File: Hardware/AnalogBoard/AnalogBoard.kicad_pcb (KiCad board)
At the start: 2 copper layers, 11 parts, among them P1 CONN_4, P2 ACH67, P3 ACH45, P4 ACH23, P5 ACH01, U1 10uf, U2 0.1uf, U3 0.1uf, U4 10uf, U5 LTC2309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

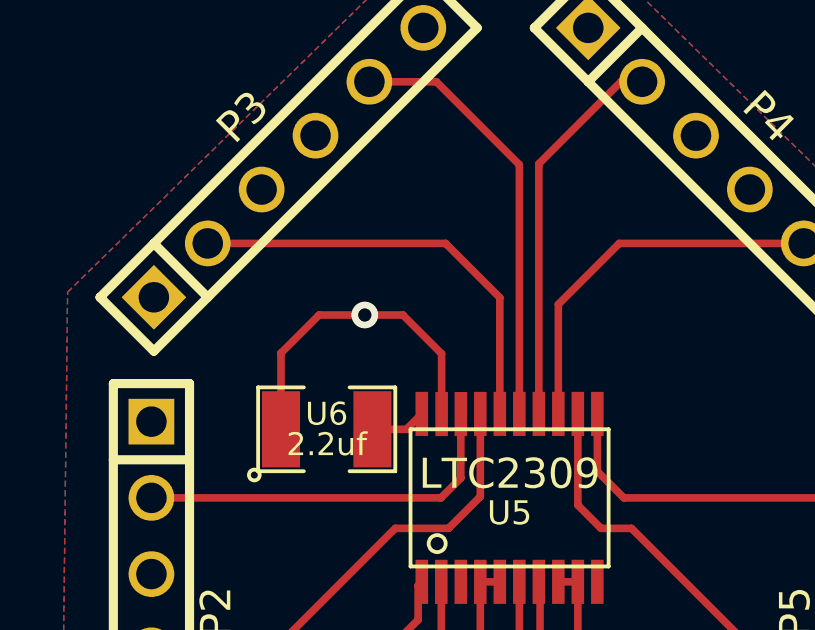
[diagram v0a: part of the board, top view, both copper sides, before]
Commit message: Changing VIA Size for the Analog Board Moving Analog Board away from Digital board connector
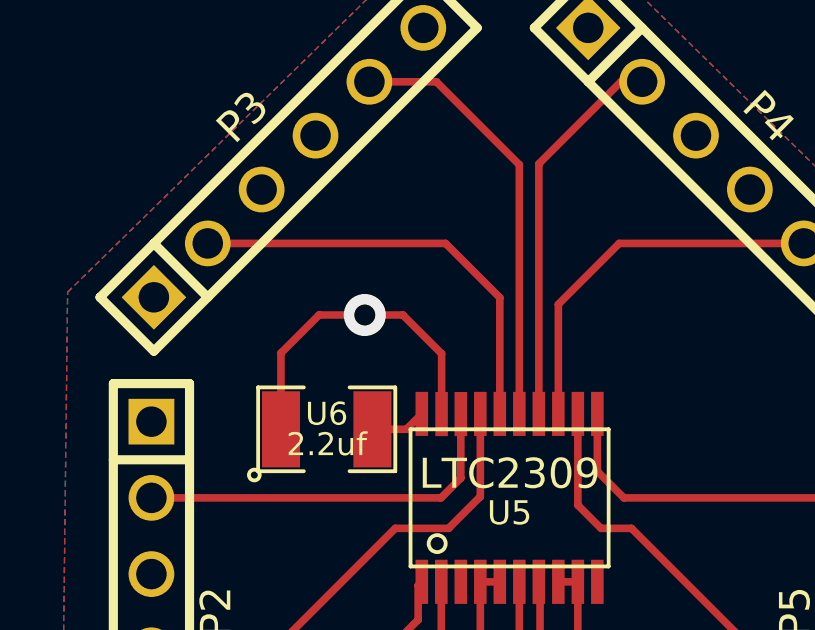
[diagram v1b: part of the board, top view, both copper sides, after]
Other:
- net class Default: via_dia 0.889 -> 1.4; via_drill 0.635 -> 1
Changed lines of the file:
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@@
     (links 44)
     (no_connects 1)
-    (area 28.448 51.816 61.468001 92.710001)
+    (area 30.226 52.832 59.9186 92.3036)
     (thickness 1.6)
     (drawings 0)
@@
     (segment_width 0.2)
     (edge_width 0.1)
-    (via_size 0.889)
-    (via_drill 0.635)
+    (via_size 1.4)
+    (via_drill 1)
     (via_min_size 0.889)
     (via_min_drill 0.508)
-    (uvia_size 0.508)
-    (uvia_drill 0.127)
+    (uvia_size 1.4)
+    (uvia_drill 1)
     (uvias_allowed no)
     (uvia_min_size 0.508)
@@
     (pad_to_mask_clearance 0)
     (aux_axis_origin 0 0)
-    (visible_elements FFFFFFBF)
+    (visible_elements 7FFFFFFF)
     (pcbplotparams
       (layerselection 3178497)
@@
     (clearance 0.254)
     (trace_width 0.254)
-    (via_dia 0.889)
-    (via_drill 0.635)
-    (uvia_dia 0.508)
-    (uvia_drill 0.127)
+    (via_dia 1.4)
+    (via_drill 1)
+    (uvia_dia 1.4)
+    (uvia_drill 1)
     (add_net "")
     (add_net +5V)
@@
   (segment (start 42.94632 66.56832) (end 41.656 65.278) (width 0.254) (layer F.Cu) (net 2))
   (segment (start 41.656 65.278) (end 40.386 65.278) (width 0.254) (layer F.Cu) (net 2))
-  (via (at 40.386 65.278) (size 0.889) (layers F.Cu B.Cu) (net 2))
+  (via (at 40.386 65.278) (size 1.4) (layers F.Cu B.Cu) (net 2))
   (segment (start 42.94632 66.56832) (end 42.94632 68.58) (width 0.254) (layer F.Cu) (net 2))
   (segment (start 38.862 65.278) (end 40.386 65.278) (width 0.254) (layer F.Cu) (net 2))

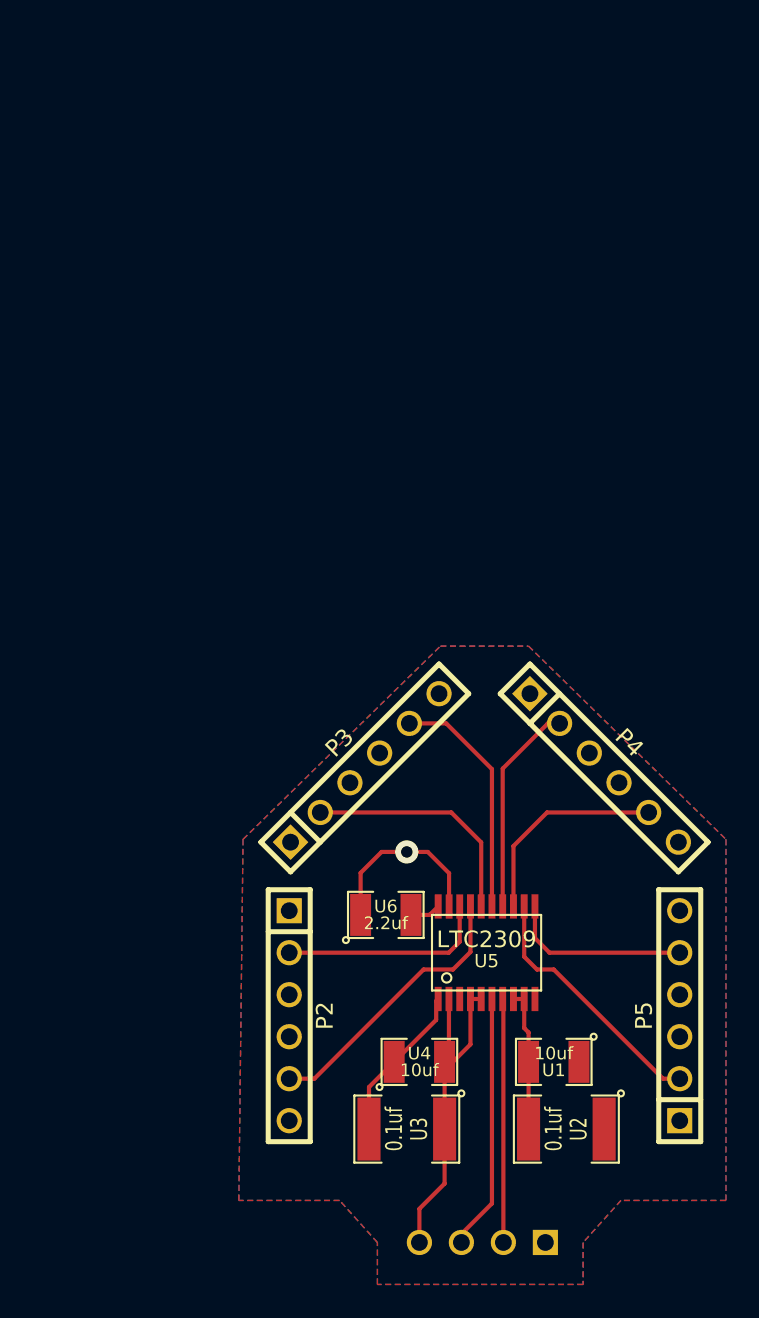
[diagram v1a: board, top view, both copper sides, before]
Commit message: Updated PCB to make it more DIY friendly Changed Vsense pin to A3 Added Design Folder
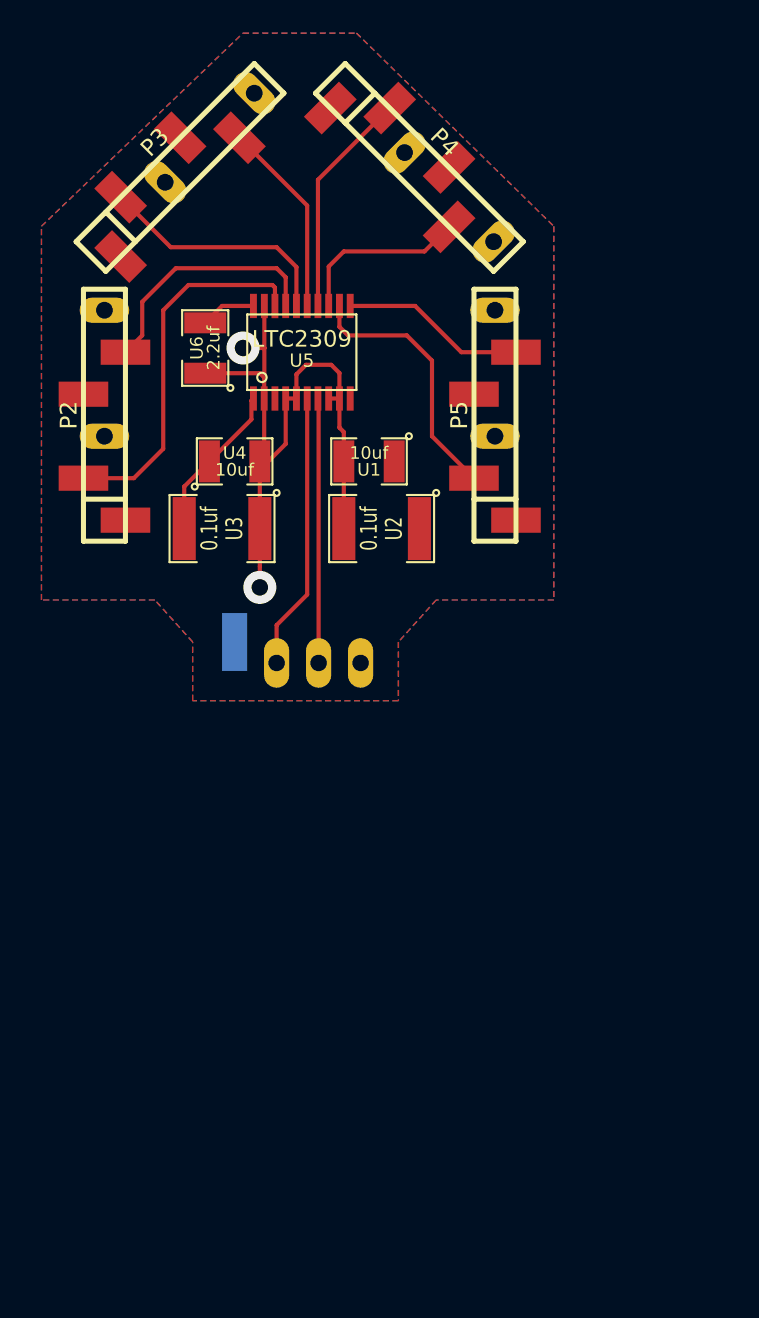
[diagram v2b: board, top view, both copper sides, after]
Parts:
- P1: footprint PIN_ARRAY_4x1 -> PIN_ARRAY_4x1_MIXED_INV
- P2, P3, P4, P5: footprint PIN_ARRAY-6X1 -> PIN_ARRAY-6X1_MIXED
- moved U3 38.0 mm to (29.2, 45.7)
- moved P2 38.0 mm to (22.1, 38.9), turned to 90 degrees
- moved P5 38.0 mm to (45.7, 38.9)
- moved U1 38.0 mm to (38.1, 41.7)
- moved U4 38.0 mm to (30.0, 41.7)
- moved U5 38.0 mm to (34.0, 35.1)
- moved P3 38.0 mm to (26.7, 23.9)
- moved P4 38.0 mm to (41.1, 23.9)
- moved U2 38.0 mm to (38.9, 45.7)
- moved P1 36.8 mm to (33.8, 53.8)
- moved U6 36.0 mm to (28.2, 34.8), turned to 90 degrees
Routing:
- net N-0000012: track 12.7 -> 22.5 mm
- net N-000005: track 14.4 -> 11.9 mm
- net N-000006: track 12.7 -> 10.7 mm
- net N-000003: track 16.9 -> 14.9 mm
- net GND: track 40.5 -> 42.2 mm, vias 1 -> 2
- net N-000008: track 1.86 -> 3.34 mm
- net SCL: track 15.5 -> 16.8 mm
- net SDA: track 14.7 -> 16.0 mm
- net N-000002: track 12.9 -> 13.8 mm
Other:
- net class Default: via_dia 1.4 -> 2

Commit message: * Updating PCB to more rectangular + Caps + On/Off Switch * Disabling Digital Breakout board for now
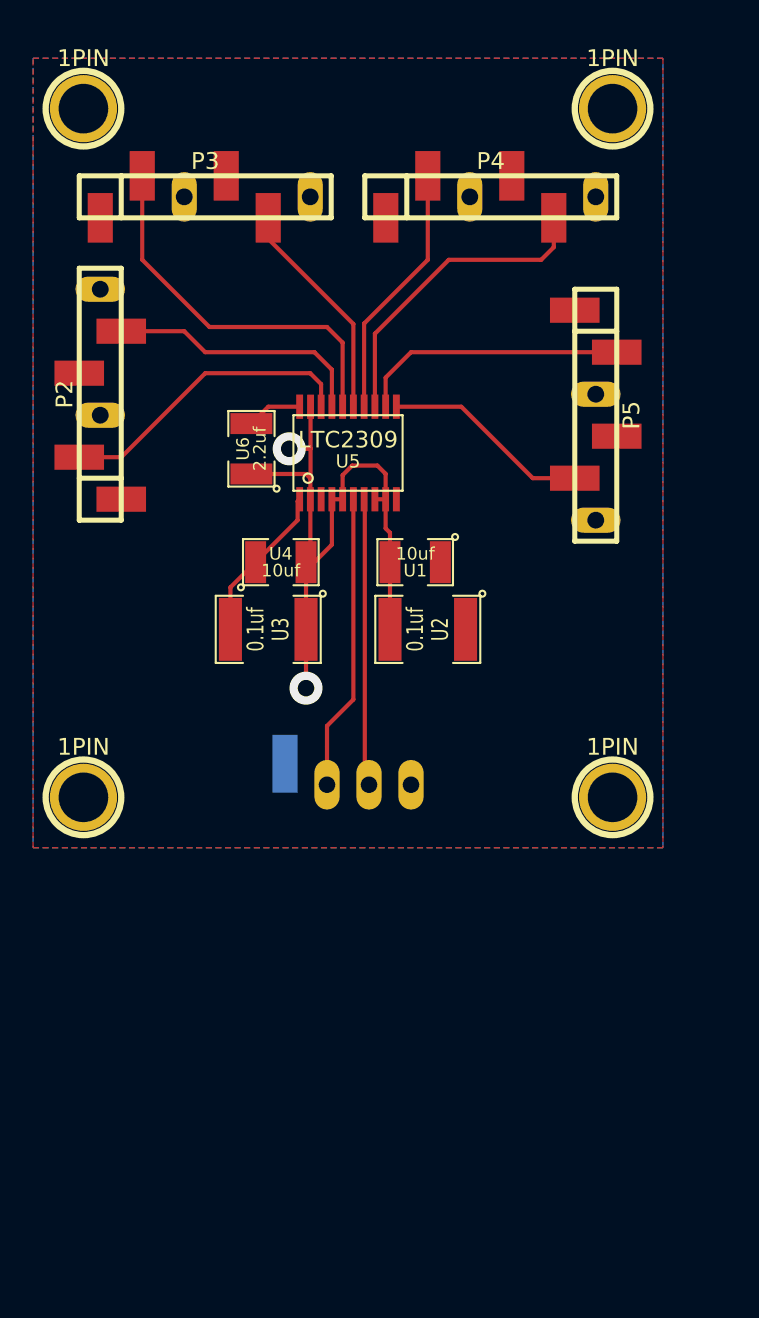
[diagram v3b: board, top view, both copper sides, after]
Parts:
- added 1PIN: P***, 1pin, F.Cu at (52.8, 62.0)
- added 1PIN: P***, 1pin, F.Cu at (20.8, 62.0)
- added 1PIN: P***, 1pin, F.Cu at (52.8, 20.3)
- added 1PIN: P***, 1pin, F.Cu at (20.8, 20.3)
- moved P1 7.97 mm to (36.8, 61.2)
- moved U1 6.71 mm to (40.9, 47.8)
- moved U2 6.71 mm to (41.7, 51.8)
- moved U3 6.71 mm to (32.0, 51.8)
- moved U4 6.71 mm to (32.8, 47.8)
- moved U5 6.71 mm to (36.8, 41.1)
- moved U6 6.71 mm to (31.0, 40.9)
- moved P5 6.10 mm to (51.8, 38.9), turned to 270 degrees
- moved P4 4.67 mm to (45.5, 25.7), turned to 0 degrees
- moved P3 2.34 mm to (28.2, 25.7), turned to 0 degrees
- moved P2 1.30 mm to (21.8, 37.6)
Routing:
- net N-000006: track 10.7 -> 19.2 mm
- net N-000004: track 14.7 -> 23.2 mm
- net N-0000012: track 22.5 -> 18.4 mm
- net N-000002: track 13.8 -> 15.6 mm
- net N-000005: track 11.9 -> 13.6 mm
- net N-000001: track 11.2 -> 12.6 mm
- net SCL: track 16.8 -> 17.9 mm
- net N-000003: track 14.9 -> 15.9 mm
- net N-000007: track 15.9 -> 16.4 mm
